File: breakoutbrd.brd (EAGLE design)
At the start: 69.3 x 99.7 mm, 6 parts

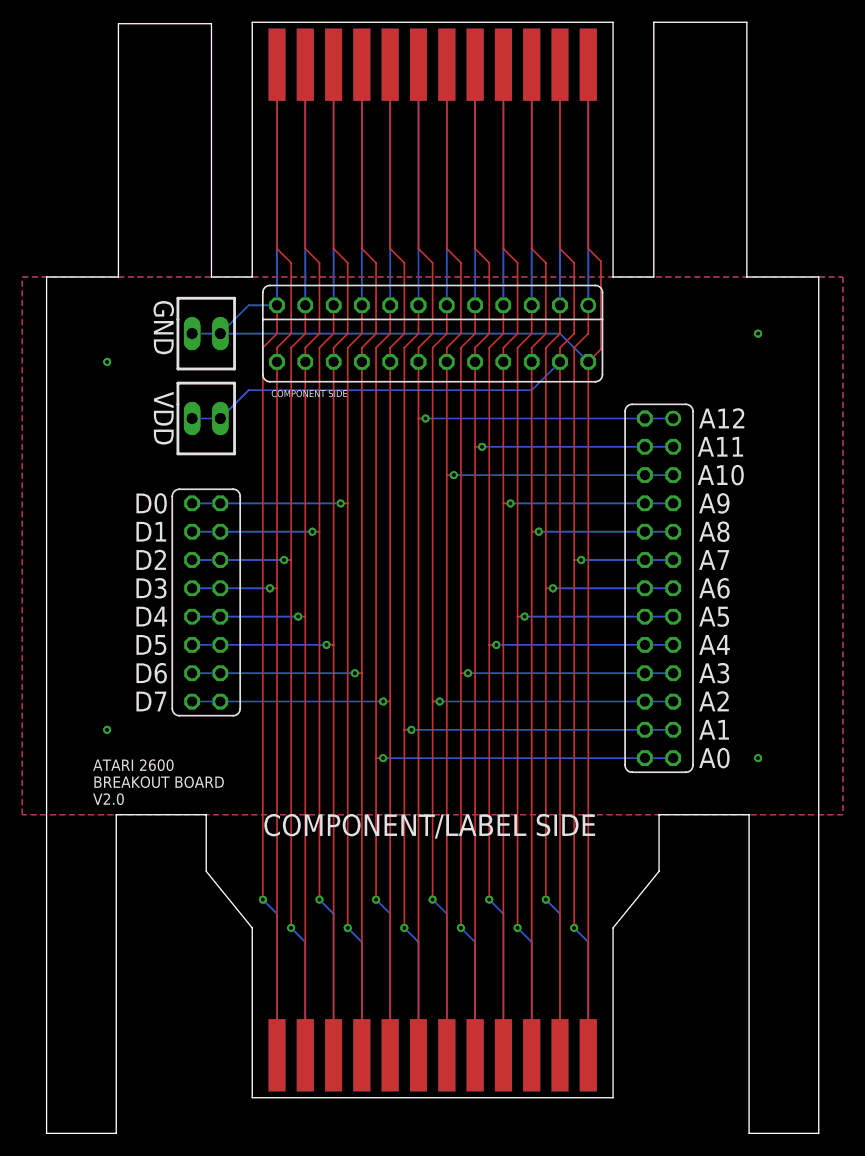
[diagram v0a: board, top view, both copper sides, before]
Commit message: more accurate prong lengths
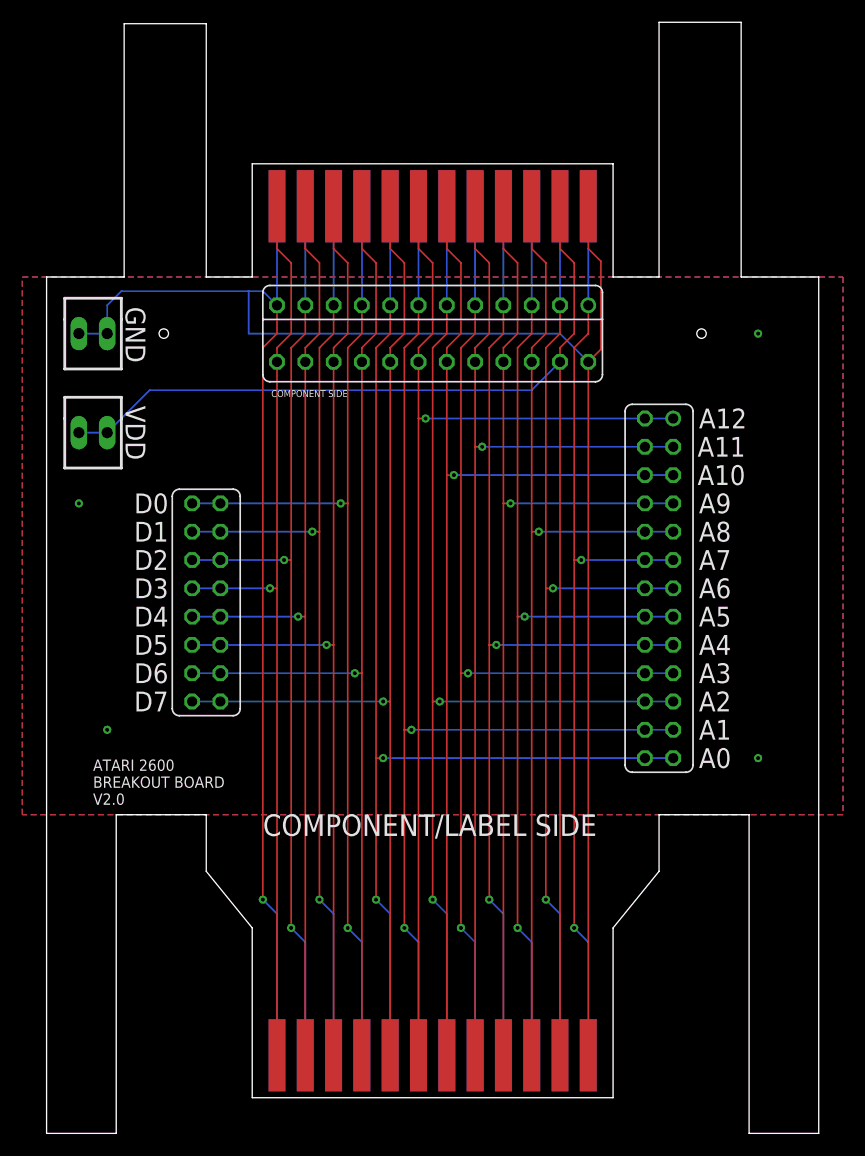
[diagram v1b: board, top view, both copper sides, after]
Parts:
- moved VDD 10.2 mm to (6.35, 59.7)
- moved GND1 10.2 mm to (6.35, 68.6)
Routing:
- net CDATA5: track 102.7 -> 90.0 mm
- net CDATA7: track 107.7 -> 95.0 mm
- net CDATA6: track 105.2 -> 92.5 mm
- net CDATA4: track 100.1 -> 87.4 mm
- net CDATA3: track 97.6 -> 84.9 mm
- net CDATA2: track 98.8 -> 86.1 mm
- net CDATA1: track 101.4 -> 88.7 mm
- net CDATA0: track 103.9 -> 91.2 mm
- net CADDR9: track 105.2 -> 92.5 mm
- net CADDR8: track 102.7 -> 90.0 mm
- net CADDR7: track 98.8 -> 86.1 mm
- net CADDR6: track 101.4 -> 88.7 mm
- net CADDR5: track 103.9 -> 91.2 mm
- net CADDR4: track 106.5 -> 93.8 mm
- net CADDR3: track 109.0 -> 96.3 mm
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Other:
- outline, holes or cut-outs redrawn

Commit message: shorten top edges set VDD on 0.1 interval
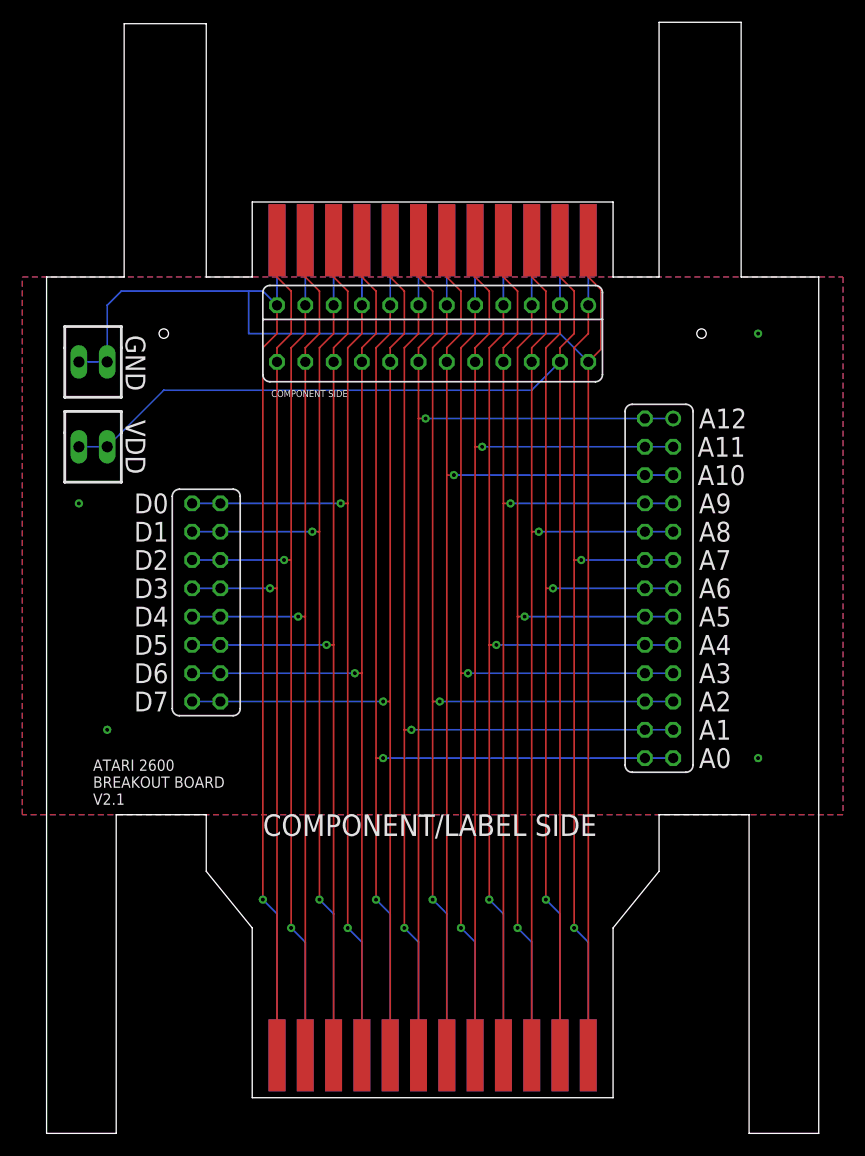
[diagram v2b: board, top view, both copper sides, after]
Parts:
- moved GND1 2.54 mm to (6.35, 66.0)
- moved VDD 1.27 mm to (6.35, 58.4)
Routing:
- net GND: track 211.1 -> 207.5 mm
- net CDATA7: track 95.0 -> 92.0 mm
- net CDATA6: track 92.5 -> 89.4 mm
- net CDATA4: track 87.4 -> 84.4 mm
- net CDATA3: track 84.9 -> 81.8 mm
- net CDATA2: track 86.1 -> 83.1 mm
- net CDATA1: track 88.7 -> 85.6 mm
- net CDATA0: track 91.2 -> 88.2 mm
- net CADDR9: track 92.5 -> 89.4 mm
- net CADDR8: track 90.0 -> 86.9 mm
- net CADDR7: track 86.1 -> 83.1 mm
- net CADDR6: track 88.7 -> 85.6 mm
- net CADDR5: track 91.2 -> 88.2 mm
- net CADDR4: track 93.8 -> 90.7 mm
- net CADDR3: track 96.3 -> 93.3 mm
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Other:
- outline, holes or cut-outs redrawn
- board text added: "ATARI 2600 BREAKOUT BOARD V2.1"
- board text removed: "ATARI 2600 BREAKOUT BOARD V2.0"
